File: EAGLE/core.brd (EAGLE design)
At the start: 20.3 x 35.6 mm, 46 parts, among them IC1 MCP1825S-3302E, Q1 MMDT3904, U2 STM32F10XCXT6, U3 SST25VF040B-S2, U4 NL17SZ125SOT553, X1 USB-MICROB, X2 IPEX-20279-001E, Y1 32Khz, Y2 8Mhz

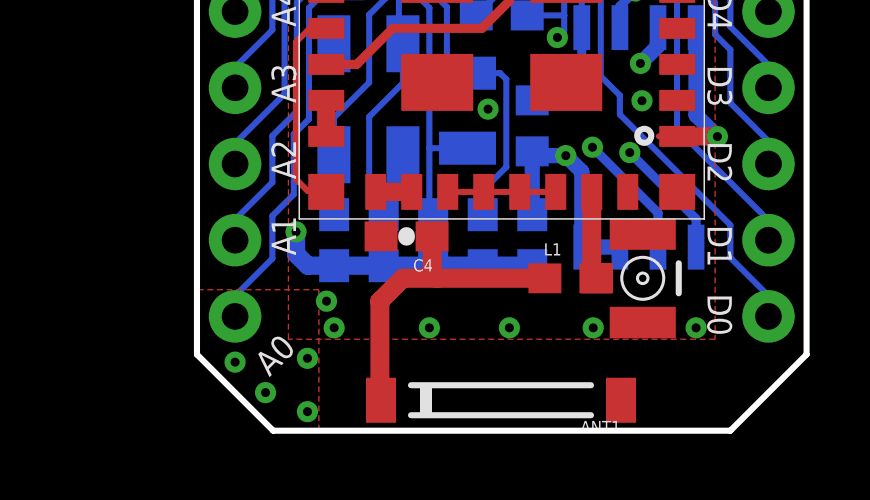
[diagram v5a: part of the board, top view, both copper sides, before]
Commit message: Cleaner, prettier RF design
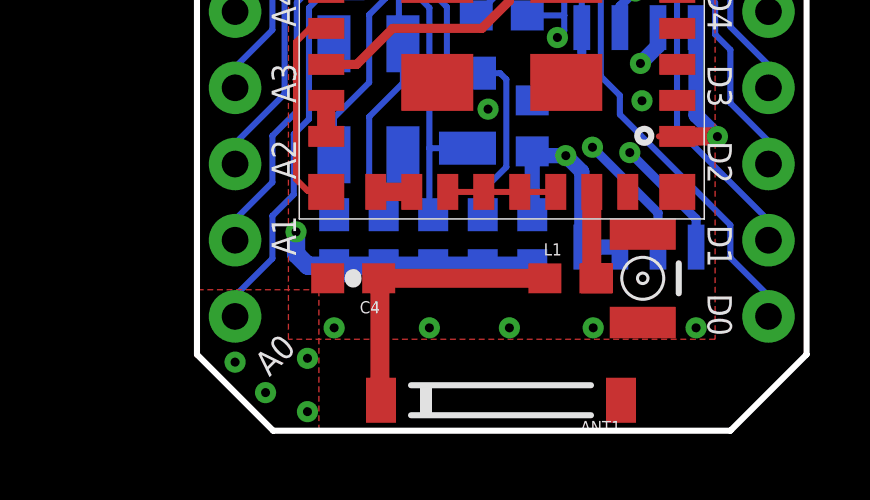
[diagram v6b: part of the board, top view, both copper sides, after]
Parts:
- moved C4 2.26 mm to (5.21, 5.08)
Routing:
- net N$3: track 10.6 -> 9.66 mm
- net GND: vias 25 -> 24
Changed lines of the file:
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@@
 </element>
 <element name="D1" library="Spark" package="DIODE-DO-220AA(SMP)" value="DIODE" x="3.048" y="34.036" locked="yes"/>
-<element name="C4" library="SparkFun-Capacitors" package="0603-CAP" value="0.8pF" x="6.985" y="6.477" rot="R180"/>
+<element name="C4" library="SparkFun-Capacitors" package="0603-CAP" value="0.8pF" x="5.207" y="5.08" rot="R180"/>
 <element name="U4" library="Spark" package="SOT-553" value="NL17SZ125SOT553" x="15.6718" y="29.21" rot="MR270"/>
 <element name="L1" library="SparkFun-Passives" package="0603" value="3.3nH" x="12.446" y="5.08"/>
@@
 <via x="9.7028" y="10.7188" extent="1-16" drill="0.3"/>
 <via x="14.8336" y="10.9982" extent="1-16" drill="0.3"/>
-<via x="4.318" y="4.318" extent="1-16" drill="0.3"/>
 <wire x1="15.506" y1="34.6202" x2="14.3002" y2="34.6202" width="0.6096" layer="1"/>
 <wire x1="14.3002" y1="34.6202" x2="14.2748" y2="34.6456" width="0.6096" layer="1"/>
@@
 <contactref element="L1" pad="1"/>
 <contactref element="C4" pad="1"/>
-<wire x1="11.596" y1="5.08" x2="8.001" y2="5.08" width="0.635" layer="1"/>
-<wire x1="8.001" y1="5.08" x2="6.858" y2="5.08" width="0.635" layer="1"/>
-<wire x1="6.858" y1="5.08" x2="6.096" y2="4.318" width="0.635" layer="1"/>
-<wire x1="6.096" y1="4.318" x2="6.096" y2="1.0546" width="0.635" layer="1"/>
+<wire x1="11.596" y1="5.08" x2="6.057" y2="5.08" width="0.635" layer="1"/>
+<wire x1="6.096" y1="5.08" x2="6.096" y2="1.0546" width="0.635" layer="1"/>
 <wire x1="6.096" y1="1.0546" x2="6.1346" y2="1.016" width="0.635" layer="1"/>
-<wire x1="7.835" y1="6.477" x2="7.835" y2="5.246" width="0.635" layer="1"/>
-<wire x1="7.835" y1="5.246" x2="8.001" y2="5.08" width="0.635" layer="1"/>
+<wire x1="6.057" y1="5.08" x2="6.096" y2="5.08" width="0.635" layer="1"/>
 </signal>
 <signal name="N$5">

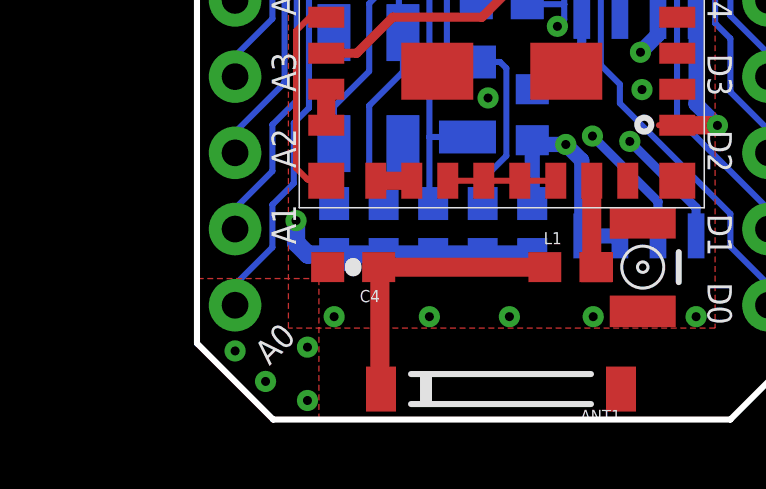
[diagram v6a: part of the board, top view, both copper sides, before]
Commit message: Fixed library part for RF capacitor
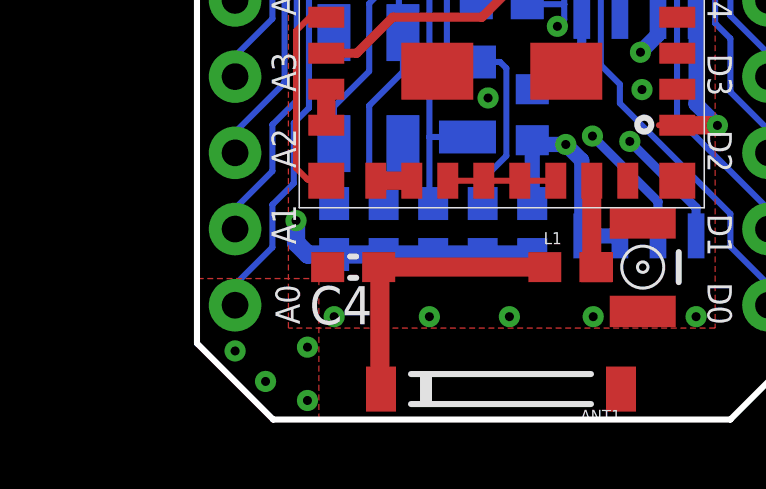
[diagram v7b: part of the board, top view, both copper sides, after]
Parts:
- C4: device SparkFun-Capacitors:0603-CAP -> rcl:C0603
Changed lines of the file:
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@@
 <wire x1="17.78" y1="3.048" x2="17.78" y2="31.75" width="0.2032" layer="51"/>
 <wire x1="2.54" y1="3.048" x2="2.54" y2="31.75" width="0.2032" layer="51"/>
-<text x="2.413" y="1.778" size="0.8128" layer="21" font="vector" ratio="15" rot="R45">A0</text>
+<text x="3.429" y="3.175" size="0.8128" layer="21" font="vector" ratio="15" rot="R90">A0</text>
 <text x="3.302" y="5.842" size="0.8128" layer="21" font="vector" ratio="15" rot="R90">A1</text>
 <text x="3.302" y="8.382" size="0.8128" layer="21" font="vector" ratio="15" rot="R90">A2</text>
@@
 </element>
 <element name="D1" library="Spark" package="DIODE-DO-220AA(SMP)" value="DIODE" x="3.048" y="34.036" locked="yes"/>
-<element name="C4" library="SparkFun-Capacitors" package="0603-CAP" value="0.8pF" x="5.207" y="5.08" rot="R180"/>
 <element name="U4" library="Spark" package="SOT-553" value="NL17SZ125SOT553" x="15.6718" y="29.21" rot="MR270"/>
 <element name="L1" library="SparkFun-Passives" package="0603" value="3.3nH" x="12.446" y="5.08"/>
+<element name="C4" library="rcl" package="C0603" value="0.8pF" x="5.207" y="5.08" rot="R180"/>
 </elements>
 <signals>
@@
 <wire x1="7.01654375" y1="18.2372" x2="9.7536" y2="18.2372" width="0.2032" layer="16"/>
 <via x="0.9144" y="33.3248" extent="1-16" drill="0.3"/>
-<contactref element="C4" pad="2"/>
 <contactref element="U1" pad="GND@11"/>
 <contactref element="U1" pad="GND@16"/>
@@
 <via x="1.27" y="2.286" extent="1-16" drill="0.3"/>
 <via x="2.286" y="1.27" extent="1-16" drill="0.3"/>
+<contactref element="C4" pad="2"/>
 </signal>
 <signal name="RAW" class="1">
@@
 <wire x1="6.135" y1="1.0164" x2="6.1346" y2="1.016" width="0.635" layer="1"/>
 <contactref element="L1" pad="1"/>
+<wire x1="6.096" y1="5.08" x2="6.096" y2="1.0546" width="0.635" layer="1"/>
+<wire x1="6.096" y1="1.0546" x2="6.1346" y2="1.016" width="0.635" layer="1"/>
 <contactref element="C4" pad="1"/>
 <wire x1="11.596" y1="5.08" x2="6.057" y2="5.08" width="0.635" layer="1"/>
-<wire x1="6.096" y1="5.08" x2="6.096" y2="1.0546" width="0.635" layer="1"/>
-<wire x1="6.096" y1="1.0546" x2="6.1346" y2="1.016" width="0.635" layer="1"/>
-<wire x1="6.057" y1="5.08" x2="6.096" y2="5.08" width="0.635" layer="1"/>
+<wire x1="6.096" y1="5.08" x2="6.057" y2="5.08" width="0" layer="19" extent="1-1"/>
 </signal>
 <signal name="N$5">

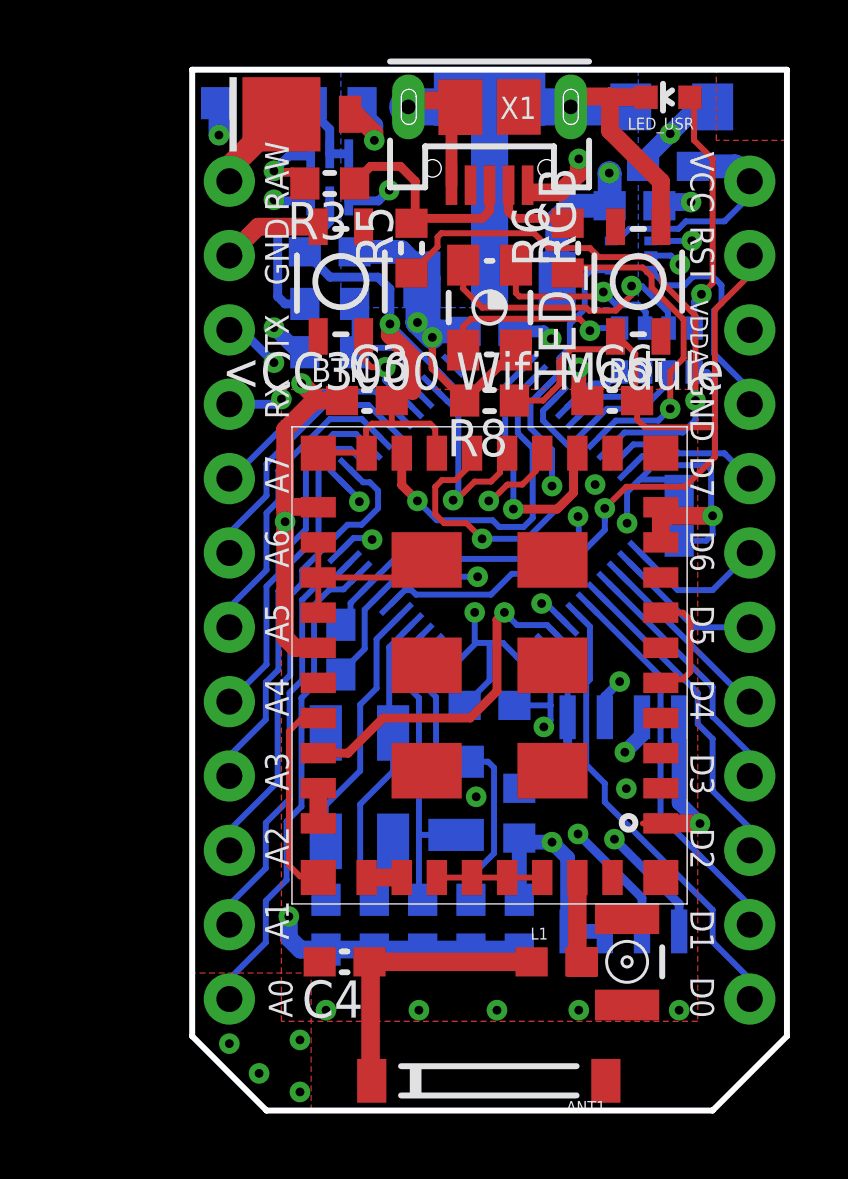
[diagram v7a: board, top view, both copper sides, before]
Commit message: updated the ufl footprint and changed the net from wifi_en to wifi_cs
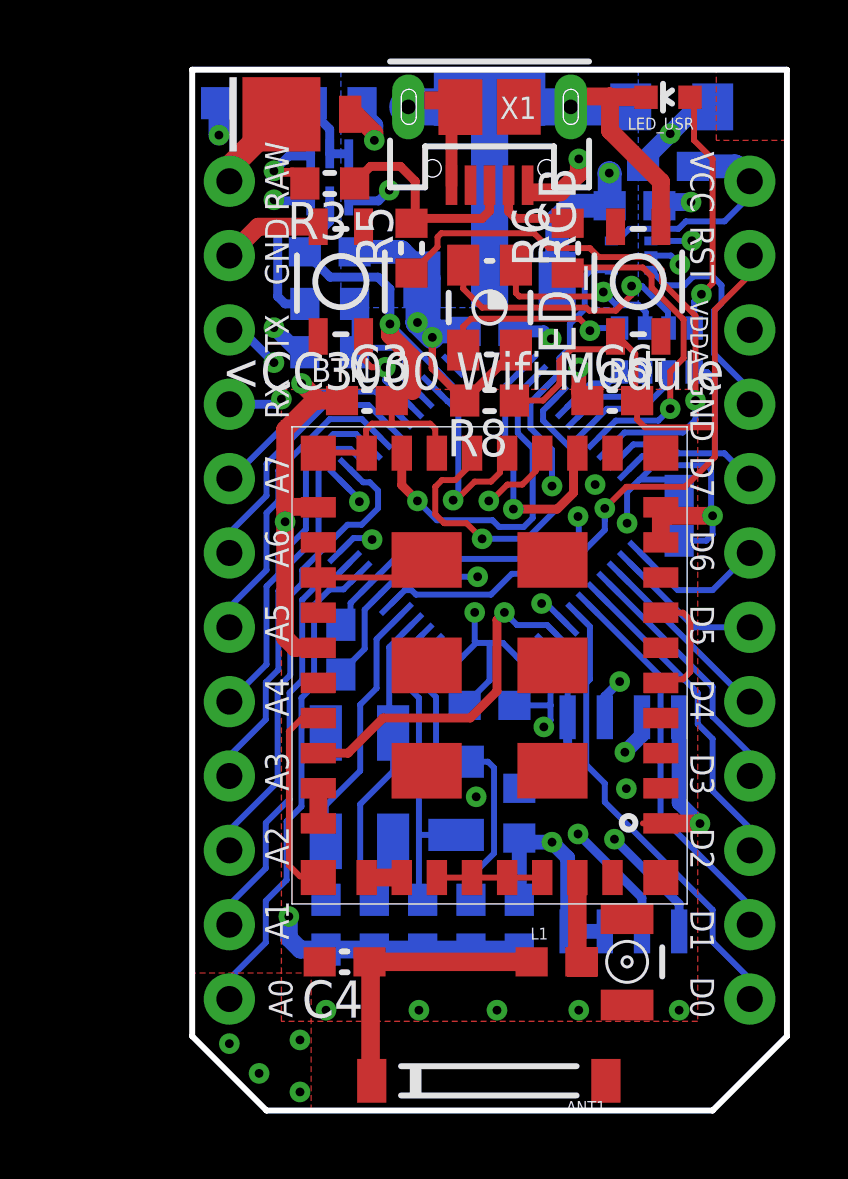
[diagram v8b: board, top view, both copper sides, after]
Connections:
- net WIFI_CS: now also U4./OE
- net WIFI_EN: no longer U4./OE
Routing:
- net WIFI_EN: track 30.9 -> 11.9 mm, vias 2 -> 1
- net WIFI_CS: track 9.35 -> 25.8 mm, vias 1 -> 2
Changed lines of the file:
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@@
 <?xml version="1.0" encoding="utf-8"?>
 <!DOCTYPE eagle SYSTEM "eagle.dtd">
-<eagle version="6.5.0">
+<eagle version="6.3">
 <drawing>
 <settings>
@@
 <setting verticaltext="up"/>
 </settings>
-<grid distance="5" unitdist="mil" unit="mil" style="lines" multiple="1" display="yes" altdistance="0.005" altunitdist="inch" altunit="inch"/>
+<grid distance="0.1" unitdist="inch" unit="inch" style="lines" multiple="1" display="yes" altdistance="0.05" altunitdist="inch" altunit="inch"/>
 <layers>
 <layer number="1" name="Top" color="4" fill="1" visible="yes" active="yes"/>
-<layer number="2" name="$GND" color="13" fill="1" visible="no" active="yes"/>
+<layer number="2" name="$GND" color="13" fill="1" visible="yes" active="yes"/>
 <layer number="3" name="Route3" color="4" fill="3" visible="no" active="no"/>
 <layer number="4" name="Route4" color="1" fill="4" visible="no" active="no"/>
@@
 <layer number="13" name="Route13" color="4" fill="5" visible="no" active="no"/>
 <layer number="14" name="Route14" color="1" fill="6" visible="no" active="no"/>
-<layer number="15" name="$+3V3" color="11" fill="1" visible="no" active="yes"/>
+<layer number="15" name="$+3V3" color="11" fill="1" visible="yes" active="yes"/>
 <layer number="16" name="Bottom" color="1" fill="1" visible="yes" active="yes"/>
 <layer number="17" name="Pads" color="2" fill="1" visible="yes" active="yes"/>
@@
 <layer number="22" name="bPlace" color="14" fill="1" visible="yes" active="yes"/>
 <layer number="23" name="tOrigins" color="15" fill="1" visible="yes" active="yes"/>
-<layer number="24" name="bOrigins" color="15" fill="1" visible="yes" active="yes"/>
+<layer number="24" name="bOrigins" color="15" fill="1" visible="no" active="yes"/>
 <layer number="25" name="tNames" color="7" fill="1" visible="no" active="yes"/>
 <layer number="26" name="bNames" color="7" fill="1" visible="no" active="yes"/>
@@
 <layer number="43" name="vRestrict" color="2" fill="10" visible="no" active="yes"/>
 <layer number="44" name="Drills" color="7" fill="1" visible="no" active="yes"/>
-<layer number="45" name="Holes" color="7" fill="1" visible="yes" active="yes"/>
+<layer number="45" name="Holes" color="7" fill="1" visible="no" active="yes"/>
 <layer number="46" name="Milling" color="3" fill="1" visible="no" active="yes"/>
 <layer number="47" name="Measures" color="7" fill="1" visible="no" active="yes"/>
@@
 <layer number="50" name="dxf" color="7" fill="1" visible="no" active="yes"/>
 <layer number="51" name="tDocu" color="6" fill="1" visible="yes" active="yes"/>
-<layer number="52" name="bDocu" color="7" fill="1" visible="no" active="yes"/>
+<layer number="52" name="bDocu" color="7" fill="1" visible="yes" active="yes"/>
 <layer number="53" name="tGND_GNDA" color="7" fill="9" visible="no" active="no"/>
 <layer number="54" name="bGND_GNDA" color="1" fill="9" visible="no" active="no"/>
@@
 <wire x1="12.126034375" y1="16.5862" x2="11.0998" y2="16.5862" width="0.2032" layer="16"/>
 <wire x1="11.0998" y1="16.5862" x2="10.668" y2="17.018" width="0.2032" layer="16"/>
-<contactref element="U4" pad="/OE"/>
-<via x="17.0688" y="29.718" extent="1-16" drill="0.3"/>
-<wire x1="15.6718" y1="29.71" x2="15.6798" y2="29.718" width="0.2032" layer="16"/>
-<wire x1="15.6718" y1="29.71" x2="17.0608" y2="29.71" width="0.2032" layer="16"/>
-<wire x1="10.2616" y1="20.1676" x2="10.7188" y2="19.7104" width="0.2032" layer="15"/>
-<wire x1="10.7188" y1="19.7104" x2="10.7188" y2="17.0688" width="0.2032" layer="15"/>
-<wire x1="10.7188" y1="17.0688" x2="10.668" y2="17.018" width="0.2032" layer="15"/>
-<wire x1="17.0608" y1="29.71" x2="17.0688" y2="29.718" width="0.2032" layer="16"/>
-<wire x1="10.2616" y1="20.1676" x2="9.9314" y2="20.1676" width="0.2032" layer="15"/>
-<wire x1="9.9314" y1="20.1676" x2="9.525" y2="20.574" width="0.2032" layer="15"/>
-<wire x1="9.525" y1="20.574" x2="9.525" y2="21.209" width="0.2032" layer="15"/>
-<wire x1="9.525" y1="21.209" x2="10.287" y2="21.971" width="0.2032" layer="15"/>
-<wire x1="10.287" y1="21.971" x2="11.303" y2="21.971" width="0.2032" layer="15"/>
-<wire x1="11.303" y1="21.971" x2="15.875" y2="26.543" width="0.2032" layer="15"/>
-<wire x1="15.875" y1="26.543" x2="15.875" y2="29.329" width="0.2032" layer="15"/>
-<wire x1="15.875" y1="29.329" x2="16.256" y2="29.71" width="0.2032" layer="15"/>
-<wire x1="16.256" y1="29.71" x2="17.0608" y2="29.71" width="0.2032" layer="15"/>
-<wire x1="17.0608" y1="29.71" x2="17.0688" y2="29.718" width="0.2032" layer="15"/>
 </signal>
 <signal name="USBM">
@@
 <wire x1="13.0302" y1="21.1074" x2="13.0302" y2="22.3302" width="0.3048" layer="1"/>
 <wire x1="13.0302" y1="22.3302" x2="13.16" y2="22.46" width="0.3048" layer="1"/>
+<contactref element="U4" pad="/OE"/>
+<via x="17.0688" y="29.718" extent="1-16" drill="0.3"/>
+<wire x1="16.256" y1="29.718" x2="15.875" y2="29.337" width="0.2032" layer="15"/>
+<wire x1="15.875" y1="29.337" x2="15.875" y2="26.543" width="0.2032" layer="15"/>
+<wire x1="15.875" y1="26.543" x2="11.303" y2="21.971" width="0.2032" layer="15"/>
+<wire x1="11.303" y1="21.971" x2="10.3124" y2="21.971" width="0.2032" layer="15"/>
+<wire x1="10.3124" y1="21.971" x2="9.525" y2="21.1836" width="0.2032" layer="15"/>
+<wire x1="9.525" y1="21.1836" x2="9.525" y2="20.574" width="0.2032" layer="15"/>
+<wire x1="9.525" y1="20.574" x2="9.9314" y2="20.1676" width="0.2032" layer="15"/>
+<wire x1="9.9314" y1="20.1676" x2="10.5918" y2="20.1676" width="0.2032" layer="15"/>
+<wire x1="10.5918" y1="20.1676" x2="10.9728" y2="20.5486" width="0.2032" layer="15"/>
+<wire x1="16.256" y1="29.718" x2="17.0688" y2="29.718" width="0.2032" layer="15"/>
+<wire x1="15.6718" y1="29.71" x2="17.0608" y2="29.71" width="0.2032" layer="16"/>
+<wire x1="17.0608" y1="29.71" x2="17.0688" y2="29.718" width="0.2032" layer="16"/>
 </signal>
 <signal name="SPI_MOSI">
@@
 <wire x1="13.16" y1="7.96" x2="13.16" y2="5.216" width="0.635" layer="1"/>
 <wire x1="13.16" y1="5.216" x2="13.296" y2="5.08" width="0.635" layer="1"/>
-<wire x1="13.296" y1="5.08" x2="13.3315" y2="5.08" width="0" layer="19" extent="1-1"/>
+<wire x1="13.296" y1="5.08" x2="13.3315" y2="5.08" width="0.2032" layer="1"/>
 </signal>
 <signal name="LED1">
@@
 <wire x1="6.096" y1="1.0546" x2="6.1346" y2="1.016" width="0.635" layer="1"/>
 <contactref element="C4" pad="1"/>
-<wire x1="11.596" y1="5.08" x2="6.057" y2="5.08" width="0.635" layer="1"/>
-<wire x1="6.096" y1="5.08" x2="6.057" y2="5.08" width="0" layer="19" extent="1-1"/>
+<wire x1="11.596" y1="5.08" x2="6.096" y2="5.08" width="0.635" layer="1"/>
+<wire x1="6.096" y1="5.08" x2="6.057" y2="5.08" width="0.635" layer="1"/>
 </signal>
 <signal name="N$5">
 </signal>
 </signals>
-<errors>
-</errors>
 </board>
 </drawing>
